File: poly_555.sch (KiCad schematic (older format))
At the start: 99 parts, among them U1 555, U10 555, U11 555, U12 555, U2 555, U3 555, U4 555, U5 555, U6 555, U7 555, U8 555, U9 555

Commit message: Hierarchal sheets and PCB layout start
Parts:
- removed C10, C11, C12, C13, C14, C15, C16, C17, C18, C19, C20, C21, C22, C23, C24, C3, C5, C6, C7, C8, C9: C, symbol Device:C
- removed C4: 10nF, symbol Device:C
- removed LS?: Speaker, symbol Device:Speaker
- removed R17, R18, R20, R22, R23, R24, R26, R28, R29, R30, R32, R34, R35: 100k, symbol Device:R
- removed R19, R21, R25, R27, R31, R33, R36: 10k, symbol Device:R
- removed RV10, RV11, RV12, RV2, RV3, RV4, RV5, RV6, RV7, RV8, RV9: R_POT_TRIM_US, symbol Device:R_POT_TRIM_US
- removed S1: FSM4JSMATR, digikey-footprints:Switch_Tactile_SMD_6x6mm, symbol dk_Tactile-Switches:FSM4JSMATR
- removed U1, U10, U11, U12, U2, U3, U4, U5, U6, U7, U8, U9: 555, digikey-footprints:DIP-8_W7.62mm, symbol dk_Clock-Timing-Programmable-Timers-and-Oscillators:NE555P
- added C3: 220uF, Capacitor_THT:CP_Radial_D8.0mm_P3.50mm, symbol Device:CP1
- added D1: LED, LED_THT:LED_D3.0mm, symbol Device:LED
- added LS1: Speaker, Buzzer_Beeper:Buzzer_D14mm_H7mm_P10mm, symbol Device:Speaker
- added S13, S14: FSM4JSMATR, digikey-footprints:Switch_Tactile_THT_6x6mm, symbol dk_Tactile-Switches:FSM4JSMATR
- added U1: LM386, digikey-footprints:DIP-8_W7.62mm, symbol Amplifier_Audio:LM386
- BT1: footprint (none) -> Connector_PinHeader_2.54mm:PinHeader_1x02_P2.54mm_Vertical
- C1: value C -> .1uF; footprint (none) -> Capacitor_THT:C_Axial_L3.8mm_D2.6mm_P7.50mm_Horizontal
- C2: value C -> .05uF; footprint (none) -> Capacitor_THT:C_Axial_L3.8mm_D2.6mm_P7.50mm_Horizontal
- R1: value 100k -> 330; footprint (none) -> Resistor_THT:R_Axial_DIN0204_L3.6mm_D1.6mm_P7.62mm_Horizontal
- R10, R12, R4, R6: footprint (none) -> Resistor_THT:R_Axial_DIN0204_L3.6mm_D1.6mm_P7.62mm_Horizontal
- R11, R13, R14, R2, R3, R5, R7, R8, R9: value 100k -> 10k; footprint (none) -> Resistor_THT:R_Axial_DIN0204_L3.6mm_D1.6mm_P7.62mm_Horizontal
- R15: value 10k -> 10; footprint (none) -> Resistor_THT:R_Axial_DIN0204_L3.6mm_D1.6mm_P7.62mm_Horizontal
- R16: value 100k -> 10; footprint (none) -> Resistor_THT:R_Axial_DIN0204_L3.6mm_D1.6mm_P7.62mm_Horizontal
- RV1: footprint (none) -> Potentiometer_THT:Potentiometer_Alpha_RD901F-40-00D_Single_Vertical
- S10, S11, S12, S2, S3, S4, S5, S6, S7, S8, S9: footprint digikey-footprints:Switch_Tactile_SMD_6x6mm -> digikey-footprints:Switch_Tactile_THT_6x6mm
- gave numbers to parts that had none: 1
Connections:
- net at C1.2: now also U1.7 (BYPASS); no longer C2.2
- net GND: now reaches BT1.2 (-), C1.1
- net GND: now also C2.2, R15.2, RV1.1, D1.1 (K), LS1.2, U1.3 (+), U1.6 (V+); no longer R1.2, R3.1
- net at R4.1, RV1.3: now also R10.1, R11.1, R12.1, R13.1, R14.1, R2.1, R3.1, R5.1, R6.1, R7.1, R8.1, R9.1; no longer RV1.2
- net at R1.1: now also S1.3, S10.1, S10.2, S11.1, S11.2, S12.1, S12.2, S2.1, S2.2, S3.1, S3.2, S4.1, S4.2, S5.1, S5.2, S6.1, S6.2, S7.1, S7.2, S8.1, S8.2, S9.1, S9.2, S13.1, S13.2, S14.1, S14.2, U1.4 (GND)
- net at C2.1: now also R16.2
- net at BT1.1 (+), S1.2 (Com): now also S1.1
- net sheet5EF17814/Out: now reaches R3.2
- net sheet5EF17814/Out: no longer RV1.1
- net sheet5EF17814/9v: now reaches S3.3, S3.4
- net sheet5EF17814/9v: no longer R7.1
- net sheet5EF2B20E/Out: now reaches R7.2
- net sheet5EF2B20E/Out: no longer R9.1
- net sheet5EF60550/Out: now reaches R9.2
- net sheet5EF259DC/9v: now reaches S5.3, S5.4
- net sheet5EF259DC/9v: no longer R13.1
- net sheet5EF60554/Out: now reaches R13.2
- net sheet5EF60554/Out: no longer R14.1
- net at R15.1: now also RV1.2, U1.2 (-)
- net sheet5EF60555/Out: now reaches R14.2
- net sheet5EF27E47/9v: now reaches S6.3, S6.4
- net sheet5EF27E47/9v: no longer R16.1
- net sheet5EF7A07A/9v: now reaches S8.3, S8.4
- net sheet5EF60551/9v: now reaches S10.3, S10.4
- net sheet5EF60553/9v: now reaches S12.3, S12.4
- net 555_astable/9v: now reaches S2.3, S2.4
- net 555_astable/9v: no longer R2.1
- net 555_astable/Out: now reaches R2.2
- net 555_astable/Out: no longer R5.1
- net sheet5EF259DC/Out: now reaches R5.2
- net sheet5EF2302B/9v: now reaches S4.3, S4.4
- net sheet5EF2302B/9v: no longer R8.1
- net sheet5EF7A07A/Out: now reaches R8.2
- net sheet5EF7A07A/Out: no longer R11.1
- net sheet5EF60552/Out: now reaches R11.2
- net sheet5EF2B20E/9v: now reaches S7.3, S7.4
- net sheet5EF60550/9v: now reaches S9.3, S9.4
- net sheet5EF60552/9v: now reaches S11.3, S11.4
- new net: D1.2 (A), R1.2
- new net: C3.1, R16.1, U1.5
- new net: C3.2, LS1.1
- new net sheet5EF2302B/Out: R4.2
- new net sheet5EF27E47/Out: R6.2
- new net sheet5EF60551/Out: R10.2
- new net sheet5EF60553/Out: R12.2
- new net sheet5EF60554/9v: S13.3, S13.4
- new net sheet5EF60555/9v: S14.3, S14.4
- no-connect marks 0 -> 2
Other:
- note added: "Optional “fake log” resistor\nhttps://sound-au.com/project01.htm"
- note added: "TODO: consider\npower jack"
- note added: "TODO: extra resistor here to “fix”\nfrequency shift from vol change?"
- note added: "TODO: replace speaker footprint"
- moved on the sheet: BT1, S1

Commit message: Fixed button layout
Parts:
- LS1: footprint Buzzer_Beeper:Buzzer_D14mm_H7mm_P10mm -> Connector_PinHeader_2.54mm:PinHeader_1x02_P2.54mm_Vertical
- S10, S11, S12, S13, S14, S2, S3, S4, S5, S6, S7, S8, S9: footprint digikey-footprints:Switch_Tactile_THT_6x6mm -> Button_Switch_THT:SW_TH_Tactile_Omron_B3F-10xx
- U1: footprint digikey-footprints:DIP-8_W7.62mm -> Package_DIP:DIP-8_W7.62mm
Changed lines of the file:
@@
 F 0 "S2" V 4950 1750 60  0000 L CNN
 F 1 "FSM4JSMATR" V 4950 1800 60  0001 L CNN
-F 2 "digikey-footprints:Switch_Tactile_THT_6x6mm" H 5150 1800 60  0001 L CNN
+F 2 "Button_Switch_THT:SW_TH_Tactile_Omron_B3F-10xx" H 5150 1800 60  0001 L CNN
 F 3 "https://www.te.com/commerce/DocumentDelivery/DDEController?Action=srchrtrv&DocNm=2-1437565-7&DocType=Customer+Drawing&DocLang=English" H 5150 1900 60  0001 L CNN
 F 4 "450-1759-1-ND" H 5150 2000 60  0001 L CNN "Digi-Key_PN"
@@
 F 0 "S3" V 4950 2750 60  0000 L CNN
 F 1 "FSM4JSMATR" V 4950 2800 60  0001 L CNN
-F 2 "digikey-footprints:Switch_Tactile_THT_6x6mm" H 5150 2800 60  0001 L CNN
+F 2 "Button_Switch_THT:SW_TH_Tactile_Omron_B3F-10xx" H 5150 2800 60  0001 L CNN
 F 3 "https://www.te.com/commerce/DocumentDelivery/DDEController?Action=srchrtrv&DocNm=2-1437565-7&DocType=Customer+Drawing&DocLang=English" H 5150 2900 60  0001 L CNN
 F 4 "450-1759-1-ND" H 5150 3000 60  0001 L CNN "Digi-Key_PN"
@@
 F 0 "S4" V 4950 3750 60  0000 L CNN
 F 1 "FSM4JSMATR" V 4950 3800 60  0001 L CNN
-F 2 "digikey-footprints:Switch_Tactile_THT_6x6mm" H 5150 3800 60  0001 L CNN
+F 2 "Button_Switch_THT:SW_TH_Tactile_Omron_B3F-10xx" H 5150 3800 60  0001 L CNN
 F 3 "https://www.te.com/commerce/DocumentDelivery/DDEController?Action=srchrtrv&DocNm=2-1437565-7&DocType=Customer+Drawing&DocLang=English" H 5150 3900 60  0001 L CNN
 F 4 "450-1759-1-ND" H 5150 4000 60  0001 L CNN "Digi-Key_PN"
@@
 F 0 "S5" V 4950 4750 60  0000 L CNN
 F 1 "FSM4JSMATR" V 4950 4800 60  0001 L CNN
-F 2 "digikey-footprints:Switch_Tactile_THT_6x6mm" H 5150 4800 60  0001 L CNN
+F 2 "Button_Switch_THT:SW_TH_Tactile_Omron_B3F-10xx" H 5150 4800 60  0001 L CNN
 F 3 "https://www.te.com/commerce/DocumentDelivery/DDEController?Action=srchrtrv&DocNm=2-1437565-7&DocType=Customer+Drawing&DocLang=English" H 5150 4900 60  0001 L CNN
 F 4 "450-1759-1-ND" H 5150 5000 60  0001 L CNN "Digi-Key_PN"
@@
 F 0 "S6" V 4950 5750 60  0000 L CNN
 F 1 "FSM4JSMATR" V 4950 5800 60  0001 L CNN
-F 2 "digikey-footprints:Switch_Tactile_THT_6x6mm" H 5150 5800 60  0001 L CNN
+F 2 "Button_Switch_THT:SW_TH_Tactile_Omron_B3F-10xx" H 5150 5800 60  0001 L CNN
 F 3 "https://www.te.com/commerce/DocumentDelivery/DDEController?Action=srchrtrv&DocNm=2-1437565-7&DocType=Customer+Drawing&DocLang=English" H 5150 5900 60  0001 L CNN
 F 4 "450-1759-1-ND" H 5150 6000 60  0001 L CNN "Digi-Key_PN"
@@
 F 0 "S7" V 4950 6750 60  0000 L CNN
 F 1 "FSM4JSMATR" V 4950 6800 60  0001 L CNN
-F 2 "digikey-footprints:Switch_Tactile_THT_6x6mm" H 5150 6800 60  0001 L CNN
+F 2 "Button_Switch_THT:SW_TH_Tactile_Omron_B3F-10xx" H 5150 6800 60  0001 L CNN
 F 3 "https://www.te.com/commerce/DocumentDelivery/DDEController?Action=srchrtrv&DocNm=2-1437565-7&DocType=Customer+Drawing&DocLang=English" H 5150 6900 60  0001 L CNN
 F 4 "450-1759-1-ND" H 5150 7000 60  0001 L CNN "Digi-Key_PN"
@@
 F 0 "S9" V 7850 1750 60  0000 L CNN
 F 1 "FSM4JSMATR" V 7850 1800 60  0001 L CNN
-F 2 "digikey-footprints:Switch_Tactile_THT_6x6mm" H 8050 1800 60  0001 L CNN
+F 2 "Button_Switch_THT:SW_TH_Tactile_Omron_B3F-10xx" H 8050 1800 60  0001 L CNN
 F 3 "https://www.te.com/commerce/DocumentDelivery/DDEController?Action=srchrtrv&DocNm=2-1437565-7&DocType=Customer+Drawing&DocLang=English" H 8050 1900 60  0001 L CNN
 F 4 "450-1759-1-ND" H 8050 2000 60  0001 L CNN "Digi-Key_PN"
@@
 F 0 "S10" V 7850 2750 60  0000 L CNN
 F 1 "FSM4JSMATR" V 7850 2800 60  0001 L CNN
-F 2 "digikey-footprints:Switch_Tactile_THT_6x6mm" H 8050 2800 60  0001 L CNN
+F 2 "Button_Switch_THT:SW_TH_Tactile_Omron_B3F-10xx" H 8050 2800 60  0001 L CNN
 F 3 "https://www.te.com/commerce/DocumentDelivery/DDEController?Action=srchrtrv&DocNm=2-1437565-7&DocType=Customer+Drawing&DocLang=English" H 8050 2900 60  0001 L CNN
 F 4 "450-1759-1-ND" H 8050 3000 60  0001 L CNN "Digi-Key_PN"
@@
 F 0 "S11" V 7850 3750 60  0000 L CNN
 F 1 "FSM4JSMATR" V 7850 3800 60  0001 L CNN
-F 2 "digikey-footprints:Switch_Tactile_THT_6x6mm" H 8050 3800 60  0001 L CNN
+F 2 "Button_Switch_THT:SW_TH_Tactile_Omron_B3F-10xx" H 8050 3800 60  0001 L CNN
 F 3 "https://www.te.com/commerce/DocumentDelivery/DDEController?Action=srchrtrv&DocNm=2-1437565-7&DocType=Customer+Drawing&DocLang=English" H 8050 3900 60  0001 L CNN
 F 4 "450-1759-1-ND" H 8050 4000 60  0001 L CNN "Digi-Key_PN"
@@
 F 0 "S12" V 7850 4750 60  0000 L CNN
 F 1 "FSM4JSMATR" V 7850 4800 60  0001 L CNN
-F 2 "digikey-footprints:Switch_Tactile_THT_6x6mm" H 8050 4800 60  0001 L CNN
+F 2 "Button_Switch_THT:SW_TH_Tactile_Omron_B3F-10xx" H 8050 4800 60  0001 L CNN
 F 3 "https://www.te.com/commerce/DocumentDelivery/DDEController?Action=srchrtrv&DocNm=2-1437565-7&DocType=Customer+Drawing&DocLang=English" H 8050 4900 60  0001 L CNN
 F 4 "450-1759-1-ND" H 8050 5000 60  0001 L CNN "Digi-Key_PN"
@@
 F 0 "S13" V 7850 5750 60  0000 L CNN
 F 1 "FSM4JSMATR" V 7850 5800 60  0001 L CNN
-F 2 "digikey-footprints:Switch_Tactile_THT_6x6mm" H 8050 5800 60  0001 L CNN
+F 2 "Button_Switch_THT:SW_TH_Tactile_Omron_B3F-10xx" H 8050 5800 60  0001 L CNN
 F 3 "https://www.te.com/commerce/DocumentDelivery/DDEController?Action=srchrtrv&DocNm=2-1437565-7&DocType=Customer+Drawing&DocLang=English" H 8050 5900 60  0001 L CNN
 F 4 "450-1759-1-ND" H 8050 6000 60  0001 L CNN "Digi-Key_PN"
@@
 F 0 "S14" V 7850 6750 60  0000 L CNN
 F 1 "FSM4JSMATR" V 7850 6800 60  0001 L CNN
-F 2 "digikey-footprints:Switch_Tactile_THT_6x6mm" H 8050 6800 60  0001 L CNN
+F 2 "Button_Switch_THT:SW_TH_Tactile_Omron_B3F-10xx" H 8050 6800 60  0001 L CNN
 F 3 "https://www.te.com/commerce/DocumentDelivery/DDEController?Action=srchrtrv&DocNm=2-1437565-7&DocType=Customer+Drawing&DocLang=English" H 8050 6900 60  0001 L CNN
 F 4 "450-1759-1-ND" H 8050 7000 60  0001 L CNN "Digi-Key_PN"
@@
 F 0 "S8" V 4950 7750 60  0000 L CNN
 F 1 "FSM4JSMATR" V 4950 7800 60  0001 L CNN
-F 2 "digikey-footprints:Switch_Tactile_THT_6x6mm" H 5150 7800 60  0001 L CNN
+F 2 "Button_Switch_THT:SW_TH_Tactile_Omron_B3F-10xx" H 5150 7800 60  0001 L CNN
 F 3 "https://www.te.com/commerce/DocumentDelivery/DDEController?Action=srchrtrv&DocNm=2-1437565-7&DocType=Customer+Drawing&DocLang=English" H 5150 7900 60  0001 L CNN
 F 4 "450-1759-1-ND" H 5150 8000 60  0001 L CNN "Digi-Key_PN"
@@
 F 0 "U1" H 13094 4004 50  0000 L CNN
 F 1 "LM386" H 13094 4095 50  0000 L CNN
-F 2 "digikey-footprints:DIP-8_W7.62mm" H 12850 4150 50  0001 C CNN
+F 2 "Package_DIP:DIP-8_W7.62mm" H 12850 4150 50  0001 C CNN
 F 3 "http://www.ti.com/lit/ds/symlink/lm386.pdf" H 12950 4250 50  0001 C CNN
 	1    12750 4050
@@
 F 0 "LS1" H 14720 4046 50  0000 L CNN
 F 1 "Speaker" H 14720 3955 50  0000 L CNN
-F 2 "Buzzer_Beeper:Buzzer_D14mm_H7mm_P10mm" H 14550 3850 50  0001 C CNN
+F 2 "Connector_PinHeader_2.54mm:PinHeader_1x02_P2.54mm_Vertical" H 14550 3850 50  0001 C CNN
 F 3 "~" H 14540 4000 50  0001 C CNN
 	1    14550 4050

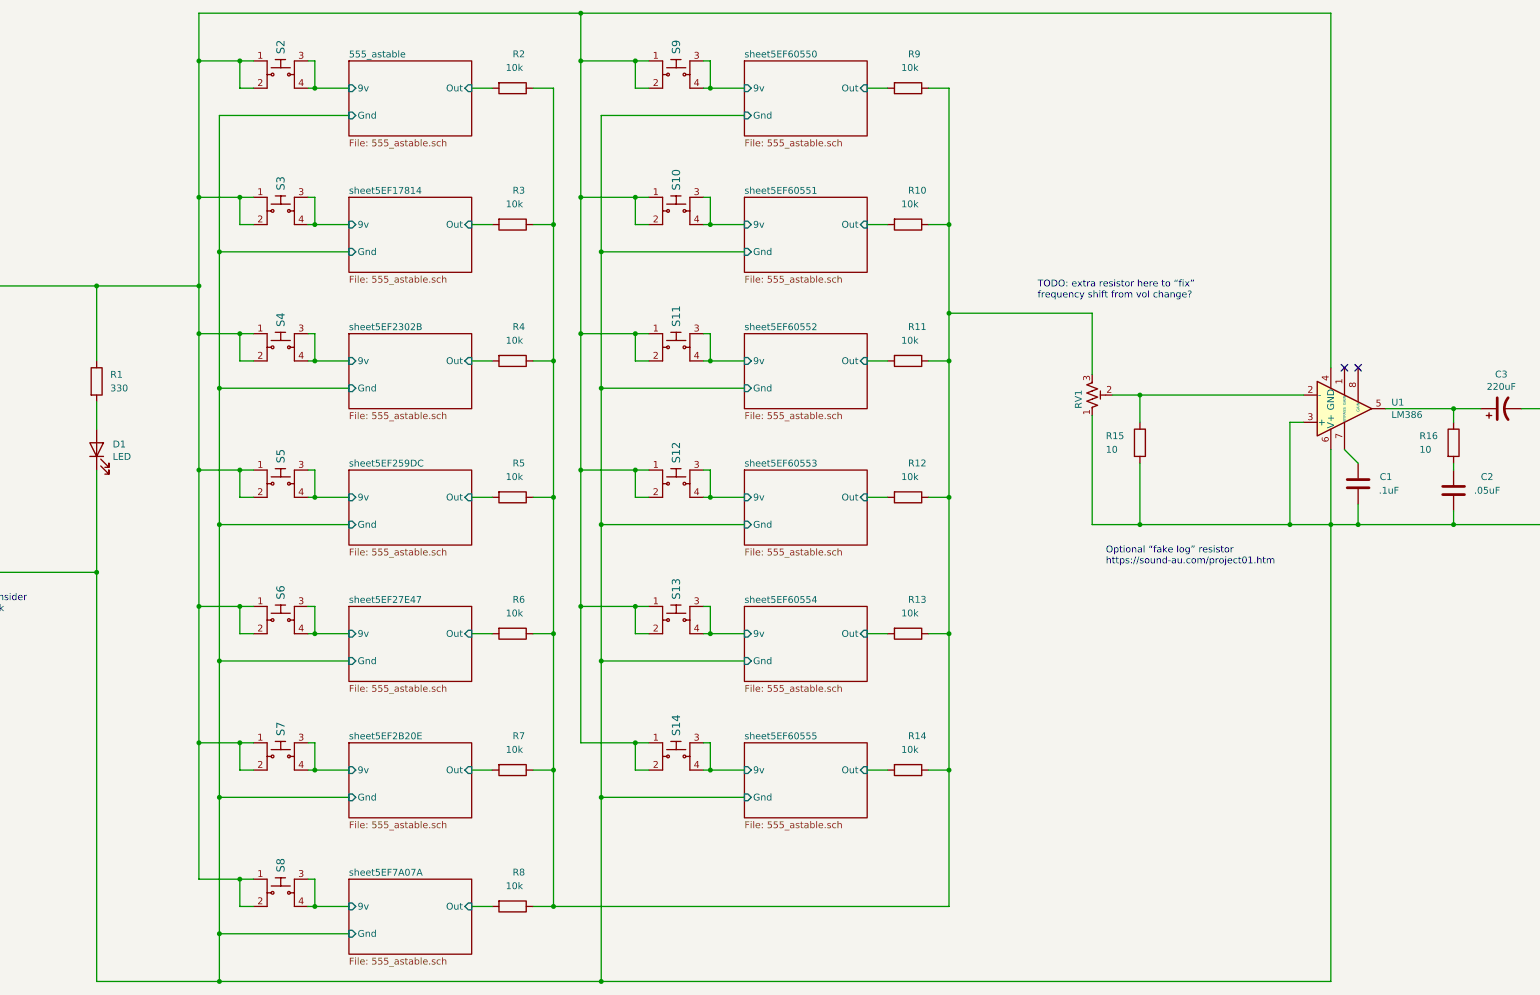
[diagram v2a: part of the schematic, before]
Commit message: Portrait layout, LEDs
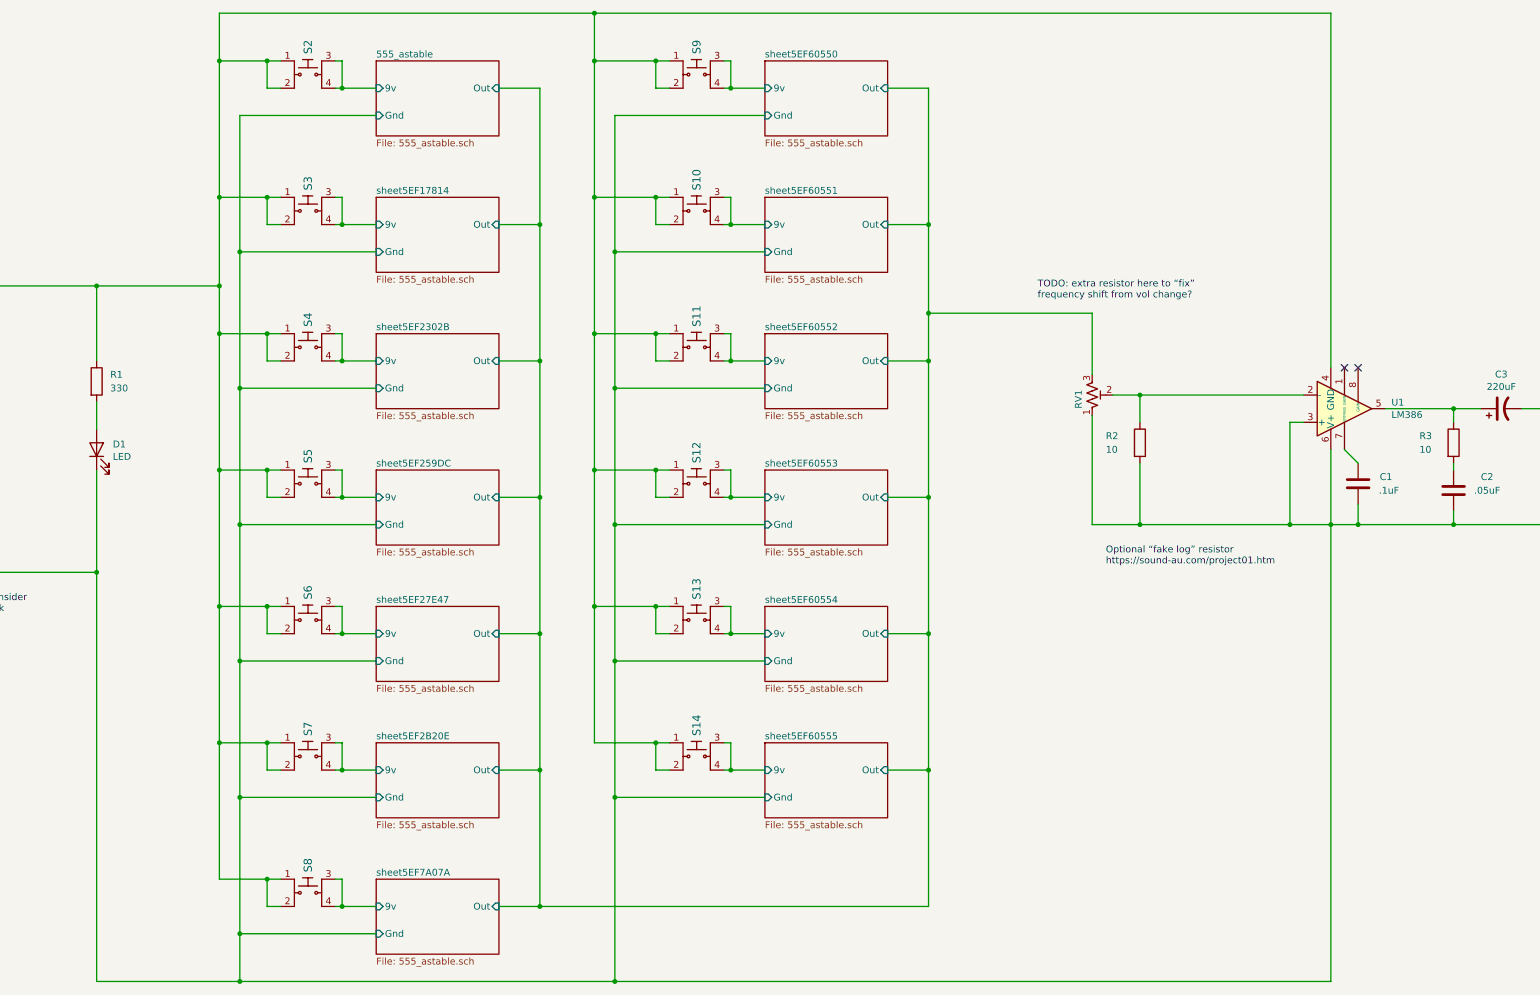
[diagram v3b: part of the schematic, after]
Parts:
- removed R10, R11, R12, R13, R14, R2, R3, R4, R5, R6, R7, R8, R9: 10k, Resistor_THT:R_Axial_DIN0204_L3.6mm_D1.6mm_P7.62mm_Horizontal, symbol Device:R
- C1, C2: footprint Capacitor_THT:C_Axial_L3.8mm_D2.6mm_P7.50mm_Horizontal -> Capacitor_THT:C_Disc_D5.0mm_W2.5mm_P5.00mm
- renumbered R15 to R2, R16 to R3
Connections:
- net 555_astable/Out: now also RV1.3
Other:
- moved on the sheet: S10, S11, S12, S13, S14, S2, S3, S4, S5, S6, S7, S8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
